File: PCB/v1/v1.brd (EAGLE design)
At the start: 55 x 39 mm, 45 parts, among them U2 AT24C512C-SHD-B

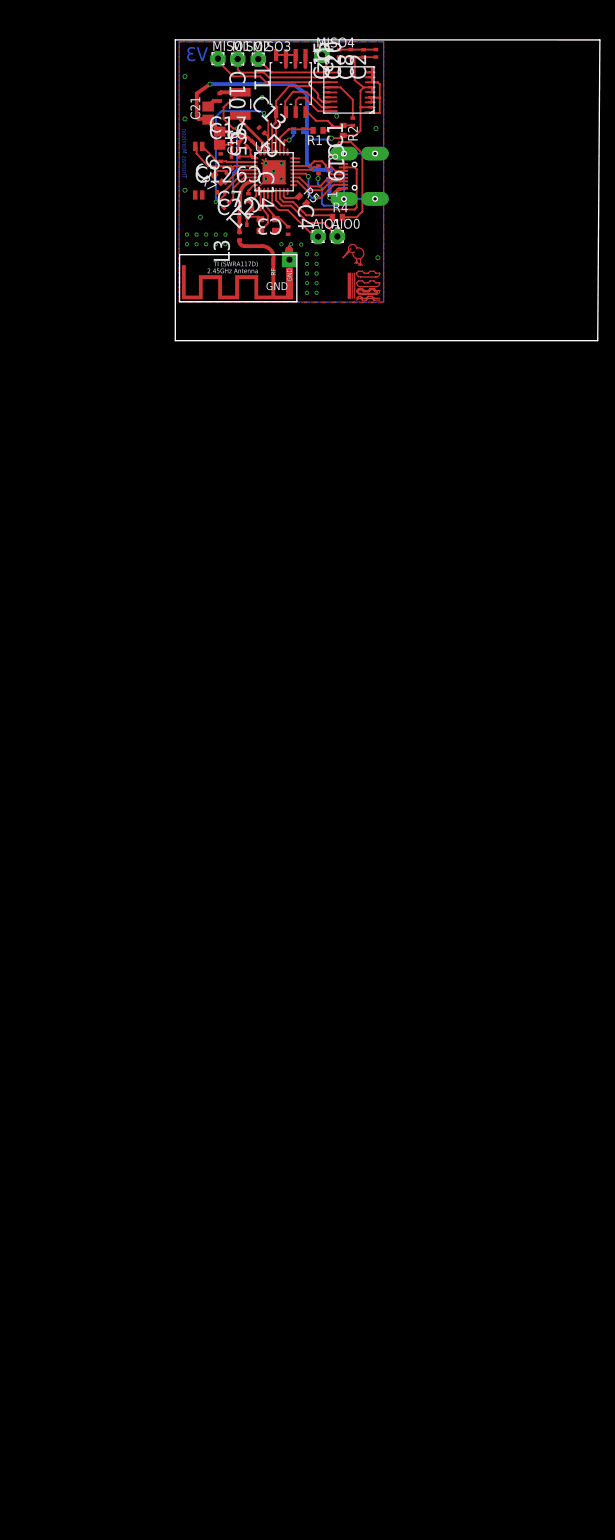
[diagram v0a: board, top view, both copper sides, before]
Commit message: added ADC and battery holder to schem
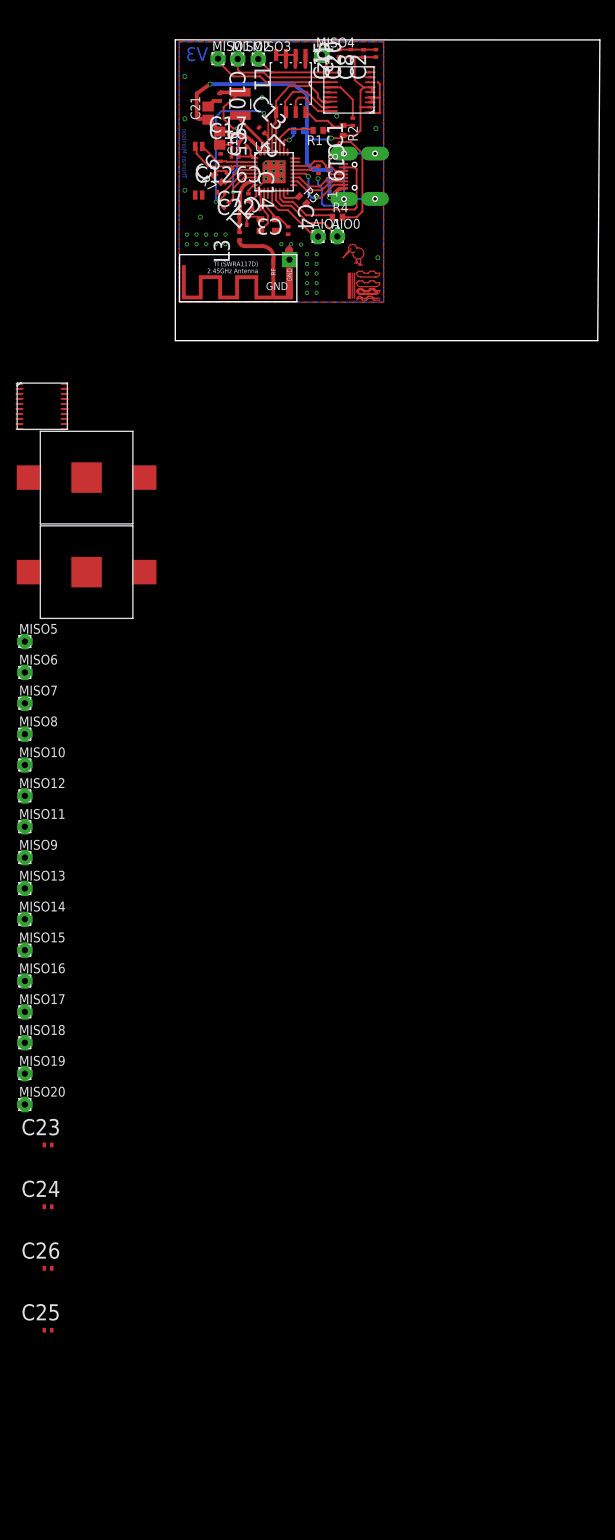
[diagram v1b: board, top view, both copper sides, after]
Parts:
- added C23, C25: 1u, AVX_By_element14_Batch_1:CAPC1005X60N
- added C24, C26: 0.1u, AVX_By_element14_Batch_1:CAPC1005X60N
- added MISO10, MISO11, MISO12, MISO13, MISO14, MISO15, MISO16, MISO17, MISO18, MISO19, MISO20, MISO5, MISO6, MISO7, MISO8, MISO9: (no value), wirepad:1,6/0,8
- added U$6: AD7997, AD7997:AD7997
- added U$7, U$8: BATTERY_2996, BATTERY_2996:BATTERY_2996
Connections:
- new net N$10: C25.1, U$6.P$06
- new net N$138: U$7.NEG, U$8.POS@1
- new net N$139: MISO5.1, U$5.P$07
- new net N$140: MISO6.1, U$5.P$08
- new net N$141: MISO7.1, U$5.P$09
- new net N$142: MISO8.1, U$5.P$010
- new net N$143: MISO9.1
- new net N$144: MISO10.1
- new net N$145: MISO11.1
- new net N$146: MISO12.1
- new net N$147: MISO13.1
- new net N$148: MISO15.1
- new net N$149: MISO14.1
- new net N$150: MISO16.1
- new net N$151: MISO17.1, U$5.P$017
- new net N$152: MISO18.1, U$5.P$016
- new net N$153: MISO19.1
- new net N$154: MISO20.1
- new net N$34: L3.1
- new net N$8: C23.1, U$6.P$02, U$6.P$05
- net GND: now also C23.2, C24.2, C25.2, C26.2, U$6.P$01, U$6.P$020, U$6.P$03, U$6.P$04; no longer U$5.P$010, U$5.P$07
- net SCL: now also U$6.P$019
- net SDA: now also U$6.P$018
- net VDD: now also U$7.POS@1
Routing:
- net GND: track 80.4 -> 76.9 mm, vias 32 -> 41
- net N$113: track 1.00 -> 0.00 mm
- net VDD: track 70.7 -> 69.8 mm
- net N$120: track 0.52 -> 0.00 mm
- net N$129: track 0.52 -> 0.00 mm

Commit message: added new ADC along with contact points
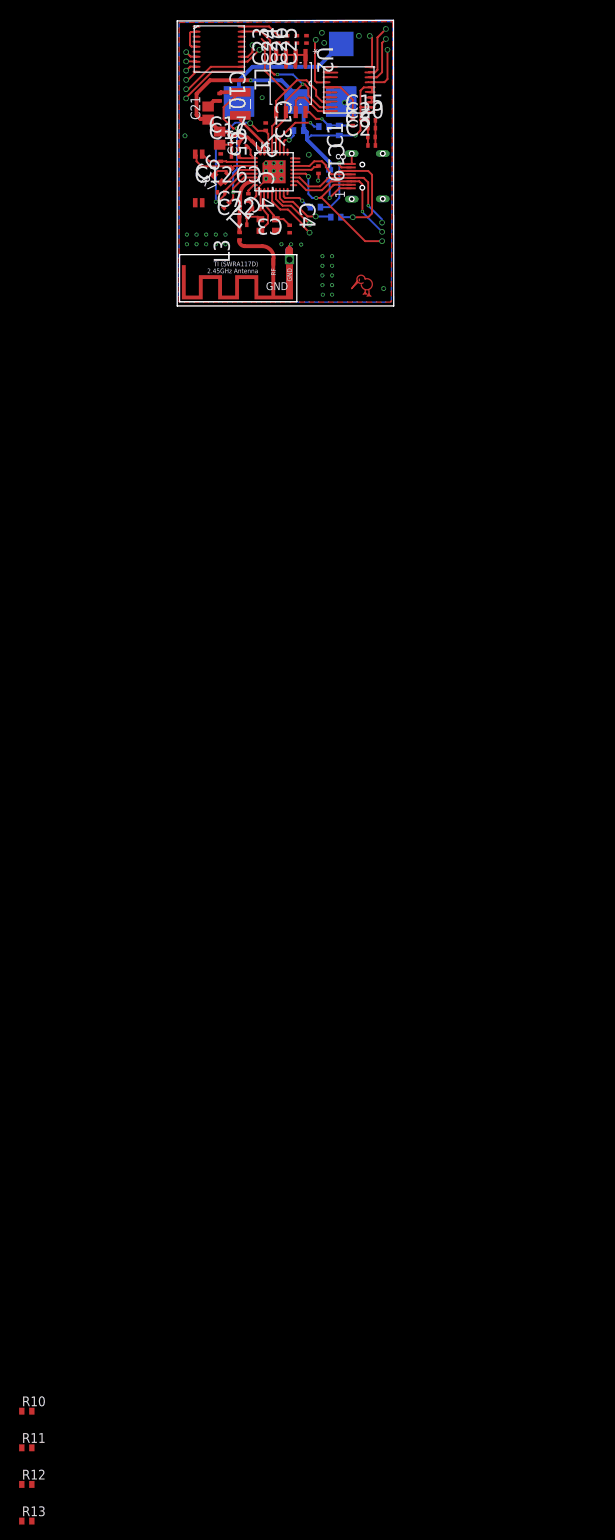
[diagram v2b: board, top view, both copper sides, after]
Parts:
- removed AIO0, AIO1, MISO1, MISO10, MISO11, MISO12, MISO13, MISO14, MISO15, MISO16, MISO17, MISO18, MISO19, MISO2, MISO20, MISO3, MISO4, MISO5, MISO6, MISO7, MISO8, MISO9: (no value), wirepad:1,6/0,8
- added R10, R11, R12, R13: 10K, rcl:R0402
- added U$10, U$11, U$12, U$13, U$14, U$15, U$16, U$17, U$18, U$19, U$20, U$21, U$22, U$23, U$24, U$25, U$26, U$27, U$28, U$29, U$30, U$9: TEST_POINT_0.5MM, TEST_POINT_0.5mm:TEST_POINT_0.5MM
- U$7, U$8: device BATTERY_2996:BATTERY_2996 -> BATTERY_2996_2:BATTERY_2996
- moved C25 170.6 mm to (17.0, 39.0), turned to 90 degrees
- moved C26 162.5 mm to (15.8, 39.0), turned to 90 degrees
- moved C24 154.4 mm to (14.5, 39.0), turned to 90 degrees
- moved C23 146.4 mm to (13.3, 39.0), turned to 90 degrees
- moved U$8 64.1 mm to (8.25, 31.0), flipped to the bottom, turned to 180 degrees
- moved U$7 58.9 mm to (21.5, 31.0), flipped to the bottom, turned to 90 degrees
- moved U$6 51.7 mm to (4.45, 37.8)
- moved C2 12.0 mm to (25.4, 25.3), turned to 0 degrees
- moved C8 10.9 mm to (25.4, 26.4), turned to 0 degrees
- moved C20 10.1 mm to (25.4, 27.6), turned to 0 degrees
- moved C15 9.66 mm to (25.4, 28.6), turned to 0 degrees
- moved R5 1.91 mm to (18.2, 17.3), flipped to the bottom, turned to 180 degrees
- moved U$2 1.00 mm to (25.6, 21.1)
- moved U$4 1.00 mm to (2.28, 23.6)
- moved R1 0.90 mm to (19.2, 27.8), flipped to the bottom, turned to 0 degrees
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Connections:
- removed net N$143: MISO9.1
- removed net N$144: MISO10.1
- removed net N$145: MISO11.1
- removed net N$146: MISO12.1
- removed net N$147: MISO13.1
- removed net N$148: MISO15.1
- removed net N$149: MISO14.1
- removed net N$150: MISO16.1
- removed net N$153: MISO19.1
- removed net N$154: MISO20.1
- new net N$106: U$12.P$2, U$6.P$011
- new net N$108: R10.2
- new net N$110: R11.2
- new net N$113: R13.2
- new net N$117: U$11.P$2, U$6.P$012
- new net N$118: U$10.P$2, U$6.P$013
- new net N$12: U$14.P$2, U$6.P$08
- new net N$137: U$6.P$014, U$9.P$2
- new net N$14: U$13.P$2, U$6.P$07
- new net N$16: U$15.P$2, U$6.P$09
- new net N$90: U$16.P$2, U$6.P$010
- net GND: now also U$7.NEG
- net N$138: now also U$7.POS@2, U$8.NEG; no longer U$7.NEG, U$8.POS@1
- net N$139: now also U$21.P$2; no longer MISO5.1
- net N$140: now also U$22.P$2; no longer MISO6.1
- net N$141: now also U$23.P$2; no longer MISO7.1
- net N$142: now also U$24.P$2; no longer MISO8.1
- net N$151: no longer MISO17.1
- net N$152: no longer MISO18.1
- net N$18: now also U$25.P$2
- net N$28: now also U$1.AIO[1], U$29.P$2; no longer AIO0.1, U$1.AIO[0]
- net N$31: now also U$27.P$2
- net N$33: now also U$1.AIO[0], U$30.P$2; no longer AIO1.1, U$1.AIO[1]
- net N$46: now also U$17.P$2; no longer MISO1.1
- net N$50: now also U$26.P$2
- net N$51: now also U$28.P$2
- net N$73: now also U$19.P$2; no longer MISO3.1
- net N$82: now also U$18.P$2; no longer MISO2.1
- net N$83: now also U$20.P$2; no longer MISO4.1
- net VDD: now also U$8.POS@2; no longer U$7.POS@1
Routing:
- net GND: track 76.9 -> 54.3 mm, vias 41 -> 37
- net N$138: track 0.00 -> 18.0 mm
- net SCL: track 15.5 -> 29.8 mm, vias 0 -> 2
- net N$82: track 13.2 -> 0.00 mm
- net N$50: track 10.0 -> 21.3 mm
- net N$46: track 17.0 -> 6.88 mm
- net N$51: track 7.64 -> 17.5 mm, vias 0 -> 1
- net N$73: track 9.54 -> 0.00 mm
- net N$31: track 7.22 -> 16.6 mm, vias 0 -> 1
- net SDA: track 15.3 -> 24.1 mm
- net N$106: track 0.76 -> 8.75 mm
- net N$20: track 20.1 -> 12.7 mm, vias 0 -> 1
- net VDD: track 69.8 -> 62.6 mm
- net VDD_CORE: track 32.7 -> 25.6 mm
- net N$141: track 0.00 -> 6.59 mm
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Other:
- board size 55 x 39 mm -> 28.1 x 37 mm
- board text removed: "Thomas Morrison"
- board text removed: "V3"

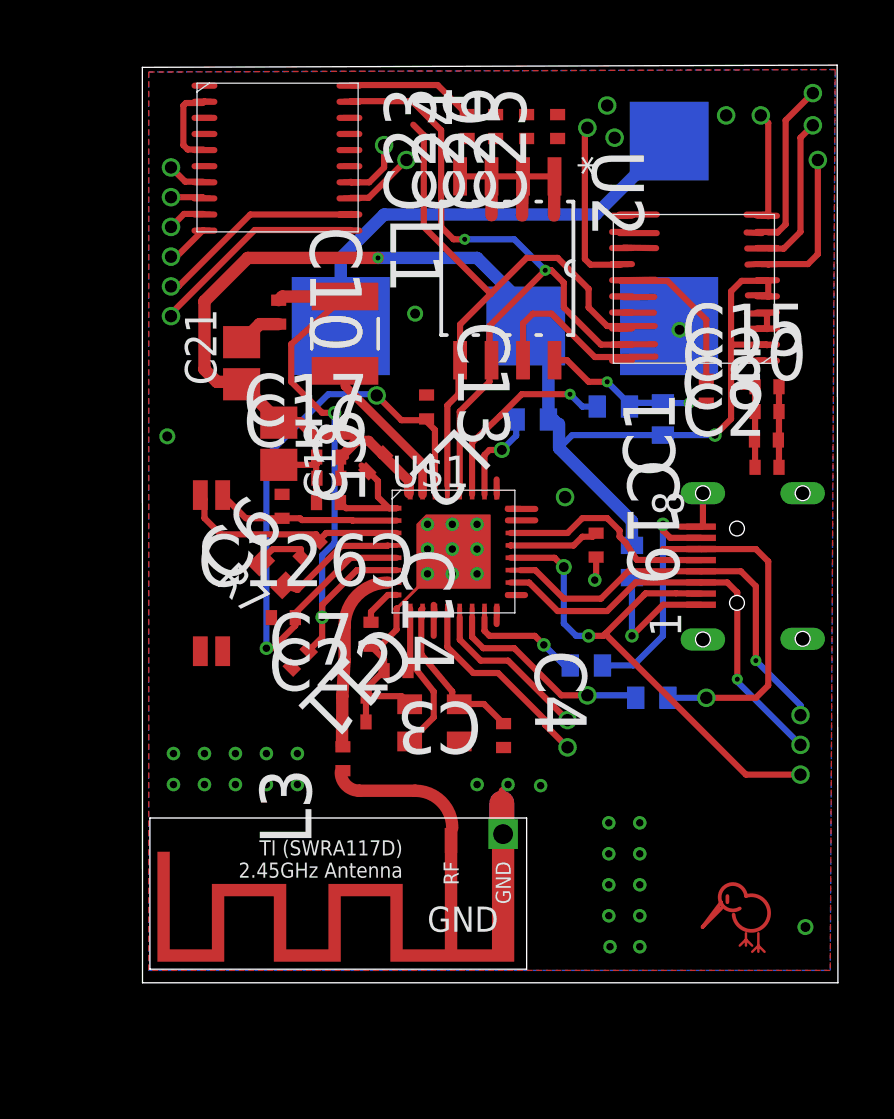
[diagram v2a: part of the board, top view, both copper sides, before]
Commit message: need to remove drill holes and go through checklist
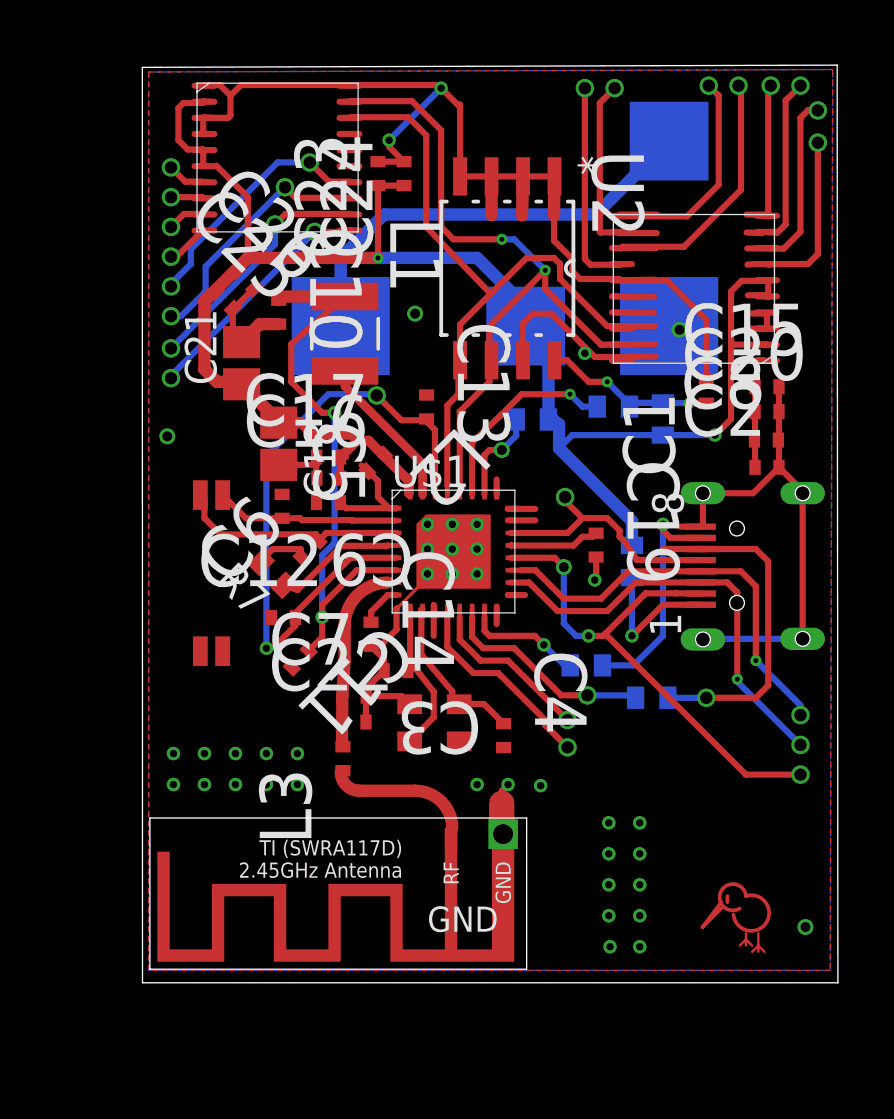
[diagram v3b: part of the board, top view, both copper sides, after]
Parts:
- moved C25 15.2 mm to (3.55, 32.0), turned to 315 degrees
- moved C26 12.9 mm to (4.42, 32.9), turned to 315 degrees
- moved U$10 11.4 mm to (1.40, 31.4)
- moved U$9 10.3 mm to (1.40, 32.6)
- moved U$18 5.36 mm to (24.3, 40.7)
- moved C24 4.16 mm to (10.8, 37.1)
- moved C23 4.07 mm to (9.75, 37.1)
- moved U$11 2.50 mm to (1.40, 30.1)
- moved U$12 2.50 mm to (1.40, 28.9)
- moved U$19 2.00 mm to (19.3, 40.6)
- moved U$17 1.60 mm to (18.1, 40.6)
- moved U$20 1.39 mm to (23.1, 40.7)
- moved U$24 1.26 mm to (25.6, 40.7)
- moved U$21 0.70 mm to (27.5, 38.4)
- moved U$22 0.63 mm to (27.5, 39.7)
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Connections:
- removed net N$10: C25.1, U$6.P$06
- removed net N$8: C23.1, U$6.P$02, U$6.P$05
- net VDD: now also C23.1, C24.1, C25.1, U$6.P$02, U$6.P$05, U$6.P$06
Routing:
- net GND: track 54.3 -> 93.2 mm, vias 37 -> 40
- net VDD: track 62.6 -> 75.1 mm
- net N$82: track 0.00 -> 10.1 mm
- net N$83: track 0.00 -> 8.64 mm
- net N$137: track 2.51 -> 10.1 mm, vias 0 -> 1
- net N$118: track 2.88 -> 10.2 mm, vias 0 -> 1
- net N$73: track 0.00 -> 6.91 mm
- net N$8: track 3.39 -> 0.00 mm
- net SDA: track 24.1 -> 26.7 mm
- net N$46: track 6.88 -> 8.44 mm
- net N$18: track 8.87 -> 10.0 mm
- net N$142: track 4.20 -> 5.32 mm
- net N$106: track 8.75 -> 9.83 mm, vias 0 -> 1
- net N$117: track 9.00 -> 9.97 mm, vias 0 -> 1
- net N$140: track 6.09 -> 7.00 mm
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
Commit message: removed connector drill holes
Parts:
- moved U$20 0.32 mm to (23.4, 40.6)
- moved U$23 0.22 mm to (26.7, 40.5)
- moved U$24 0.14 mm to (25.5, 40.6)
- moved U$18 0.14 mm to (24.4, 40.6)
- moved U$2 0.12 mm to (25.5, 21.1)
- moved U$22 0.10 mm to (27.4, 39.7)
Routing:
- net GND: track 93.2 -> 97.5 mm
- net VDD: track 75.1 -> 77.7 mm
- net N$115: track 1.75 -> 0.00 mm
- net N$8: track 0.00 -> 1.14 mm

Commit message: final checked + silk screen
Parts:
- removed R10, R11, R12, R13: 10K, rcl:R0402
- added U$31: TEST_POINT_0.5MM, TEST_POINT_0.5mm:TEST_POINT_0.5MM
- moved U$4 4.63 mm to (1.78, 19.0)
- moved C25 4.50 mm to (3.35, 27.5)
- moved C26 4.50 mm to (4.22, 28.4)
- moved U$14 4.50 mm to (1.20, 31.7)
- moved C14 4.50 mm to (9.27, 14.1)
- moved R5 4.50 mm to (18.0, 12.8)
- moved C1 4.50 mm to (22.8, 23.9)
- moved C10 4.50 mm to (5.54, 27.1)
- moved C12 4.50 mm to (5.74, 14.7)
- moved C13 4.50 mm to (11.5, 23.2)
- moved C15 4.50 mm to (25.2, 24.1)
- moved C16 4.50 mm to (7.57, 20.4)
- moved C17 4.50 mm to (7.56, 21.2)
- moved C18 4.50 mm to (5.55, 21.8)
- moved C19 4.50 mm to (18.4, 17.7)
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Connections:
- removed net N$108: R10.2
- removed net N$110: R11.2
- removed net N$113: R13.2
- net N$49: now also U$31.P$2
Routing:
- net N$125: track 0.00 -> 6.60 mm
- net N$109: track 5.43 -> 0.00 mm
- net GND: track 97.5 -> 101.6 mm, vias 40 -> 52
- net N$49: track 4.97 -> 6.89 mm
- net N$126: track 0.00 -> 1.55 mm
- net N$8: track 1.14 -> 0.00 mm
- net N$20: track 12.3 -> 13.4 mm
- net N$110: track 0.00 -> 0.94 mm
- net N$113: track 0.00 -> 0.92 mm
- net N$127: track 0.00 -> 0.91 mm
- net VDD: track 77.7 -> 78.6 mm
- net N$128: track 0.00 -> 0.90 mm
- net N$116: track 0.86 -> 0.00 mm
- net N$129: track 0.00 -> 0.86 mm
- net N$143: track 0.00 -> 0.83 mm
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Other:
- board size 28.1 x 37 mm -> 28 x 36.9 mm

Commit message: submitting for fabrication
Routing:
- net N$131: track 2.31 -> 0.00 mm
- net GND: track 101.6 -> 103.5 mm, vias 52 -> 53
- net N$130: track 1.46 -> 0.00 mm
- net N$134: track 1.46 -> 0.00 mm
- net N$133: track 1.21 -> 0.00 mm
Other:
- board text added: "CON"
- board text added: "EEG"
- board text added: "Thomas Morrison"

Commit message: PCB done and sent off. Fab confirms in production
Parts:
- moved C1 0.05 mm to (22.8, 23.9)
- moved C12 0.05 mm to (5.68, 14.7)
- moved C15 0.05 mm to (25.2, 24.1)
- moved C16 0.05 mm to (7.52, 20.4)
- moved C19 0.05 mm to (18.3, 17.7)
- moved C2 0.05 mm to (25.2, 20.8)
- moved C20 0.05 mm to (25.2, 23.1)
- moved C22 0.05 mm to (8.54, 10.5)
- moved C23 0.05 mm to (9.50, 32.6)
- moved C3 0.05 mm to (10.2, 12.6)
- moved C7 0.05 mm to (8.54, 11.6)
- moved C8 0.05 mm to (25.2, 21.9)
- moved GND 0.05 mm to (16.3, 6.45)
- moved L1 0.05 mm to (8.17, 26.2)
- moved L2 0.05 mm to (9.41, 21.0)
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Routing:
- net GND: track 103.5 -> 102.9 mm
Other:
- outline, holes or cut-outs redrawn
